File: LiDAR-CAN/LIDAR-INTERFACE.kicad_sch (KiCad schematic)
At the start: 0 parts

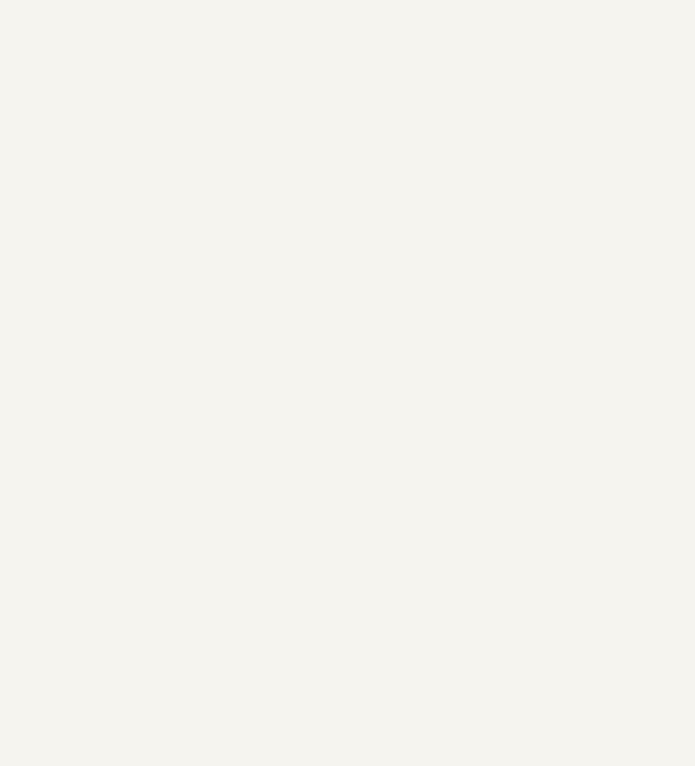
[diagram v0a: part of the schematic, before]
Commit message: Add main components in schematic sheets
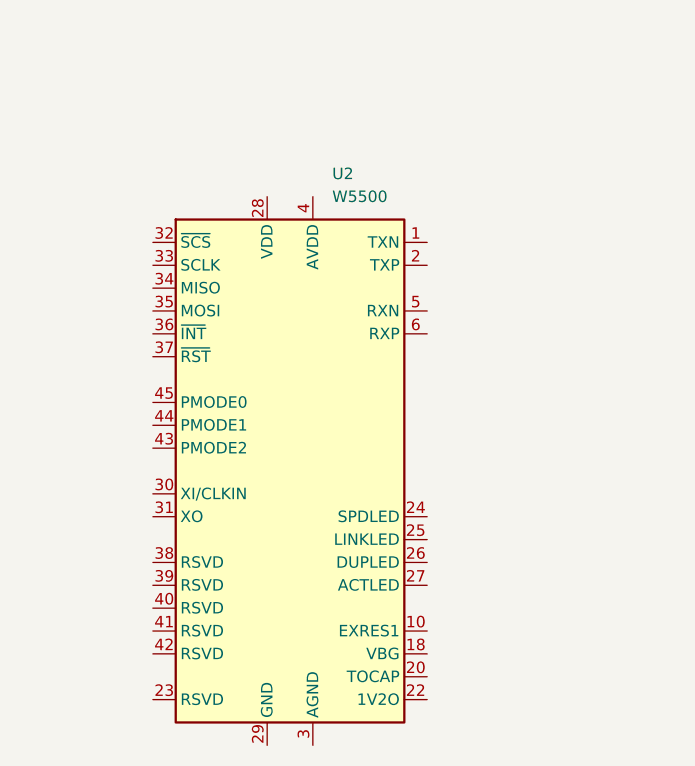
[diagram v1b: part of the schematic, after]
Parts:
- added U2: W5500, Package_QFP:LQFP-48_7x7mm_P0.5mm, symbol Interface_Ethernet:W5500
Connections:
- new net: U2.11 (AVDD), U2.15 (AVDD), U2.17 (AVDD), U2.21 (AVDD), U2.4 (AVDD), U2.8 (AVDD)
- new net: U2.14 (AGND), U2.16 (AGND), U2.19 (AGND), U2.3 (AGND), U2.48 (AGND), U2.9 (AGND)
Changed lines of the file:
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@@
+		)
+	)
+	(symbol
+		(lib_id "Interface_Ethernet:W5500")
+		(at 139.7 91.44 0)
+		(unit 1)
+		(exclude_from_sim no)
+		(in_bom yes)
+		(on_board yes)
+		(dnp no)
+		(fields_autoplaced yes)
+		(property "Reference" "U2"
+			(at 144.3833 58.42 0)
+			(effects
+				(font
+					(size 1.27 1.27)
+				)
+				(justify left)
+			)
+		)
+		(property "Value" "W5500"
+			(at 144.3833 60.96 0)
+			(effects
+				(font
+					(size 1.27 1.27)
+				)
+				(justify left)
+			)
+		)
+		(property "Footprint" "Package_QFP:LQFP-48_7x7mm_P0.5mm"
+			(at 139.7 49.53 0)
+			(effects
+				(font
+					(size 1.27 1.27)
+				)
+				(hide yes)
+			)
+		)
+		(property "Datasheet" "http://wizwiki.net/wiki/lib/exe/fetch.php/products:w5500:w5500_ds_v109e.pdf"
+			(at 139.7 66.04 0)
+			(effects
+				(font
+					(size 1.27 1.27)
+				)
+				(hide yes)
+			)
+		)
+		(property "Description" "10/100Mb SPI Ethernet controller with TCP/IP stack, LQFP-48"
+			(at 139.7 91.44 0)
+			(effects
+				(font
+					(size 1.27 1.27)
+				)
+				(hide yes)
+			)
+		)
+		(pin "32"
+		)
+		(pin "33"
+		)
+		(pin "35"
+		)
+		(pin "36"
+		)
+		(pin "37"
+		)
+		(pin "34"
+		)
+		(pin "15"
+		)
+		(pin "4"
+		)
+		(pin "42"
+		)
+		(pin "23"
+		)
+		(pin "28"
+		)
+		(pin "44"
+		)
+		(pin "29"
+		)
+		(pin "40"
+		)
+		(pin "41"
+		)
+		(pin "17"
+		)
+		(pin "21"
+		)
+		(pin "11"
+		)
+		(pin "8"
+		)
+		(pin "14"
+		)
+		(pin "16"
+		)
+		(pin "45"
+		)
+		(pin "31"
+		)
+		(pin "30"
+		)
+		(pin "38"
+		)
+		(pin "43"
+		)
+		(pin "39"
+		)
+		(pin "5"
+		)
+		(pin "7"
+		)
+		(pin "1"
+		)
+		(pin "22"
+		)
+		(pin "27"
+		)
+		(pin "26"
+		)
+		(pin "12"
+		)
+		(pin "10"
+		)
+		(pin "24"
+		)
+		(pin "3"
+		)
+		(pin "20"
+		)
+		(pin "13"
+		)
+		(pin "47"
+		)
+		(pin "19"
+		)
+		(pin "48"
+		)
+		(pin "9"
+		)
+		(pin "18"
+		)
+		(pin "46"
+		)
+		(pin "2"
+		)
+		(pin "6"
+		)
+		(pin "25"
+		)
+		(instances
+			(project ""
+				(path "/56db6f21-0e4a-4321-bd8a-db37f1842dd9/91fe436f-7e8c-47e0-899c-e39330e04729"
+					(reference "U2")
+					(unit 1)
+				)
+			)
 		)
 	)

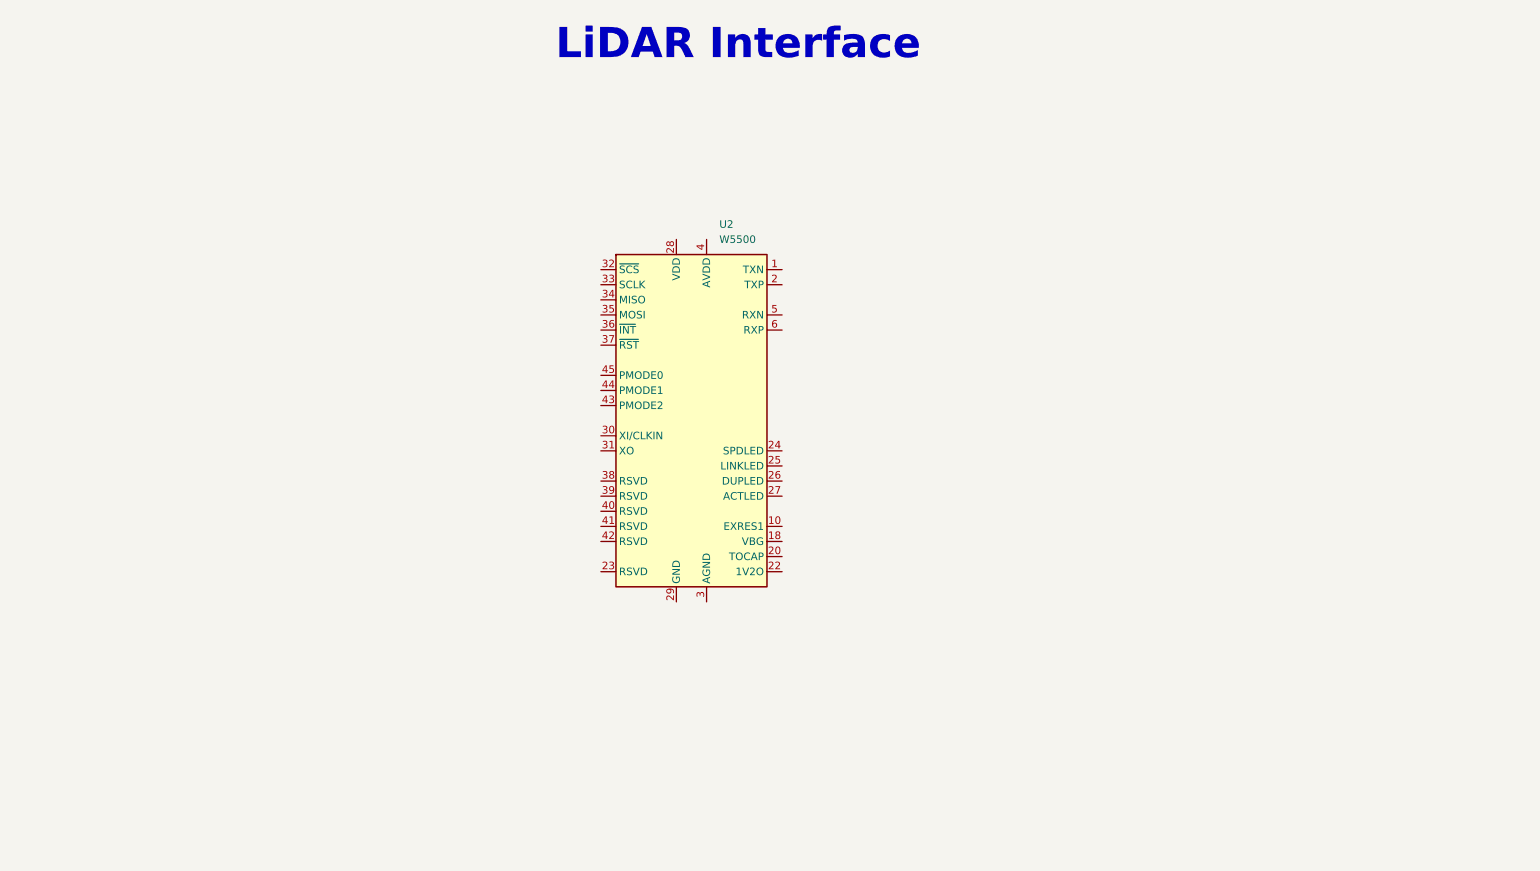
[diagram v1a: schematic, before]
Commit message: Add LiDAR Interface complete circuit
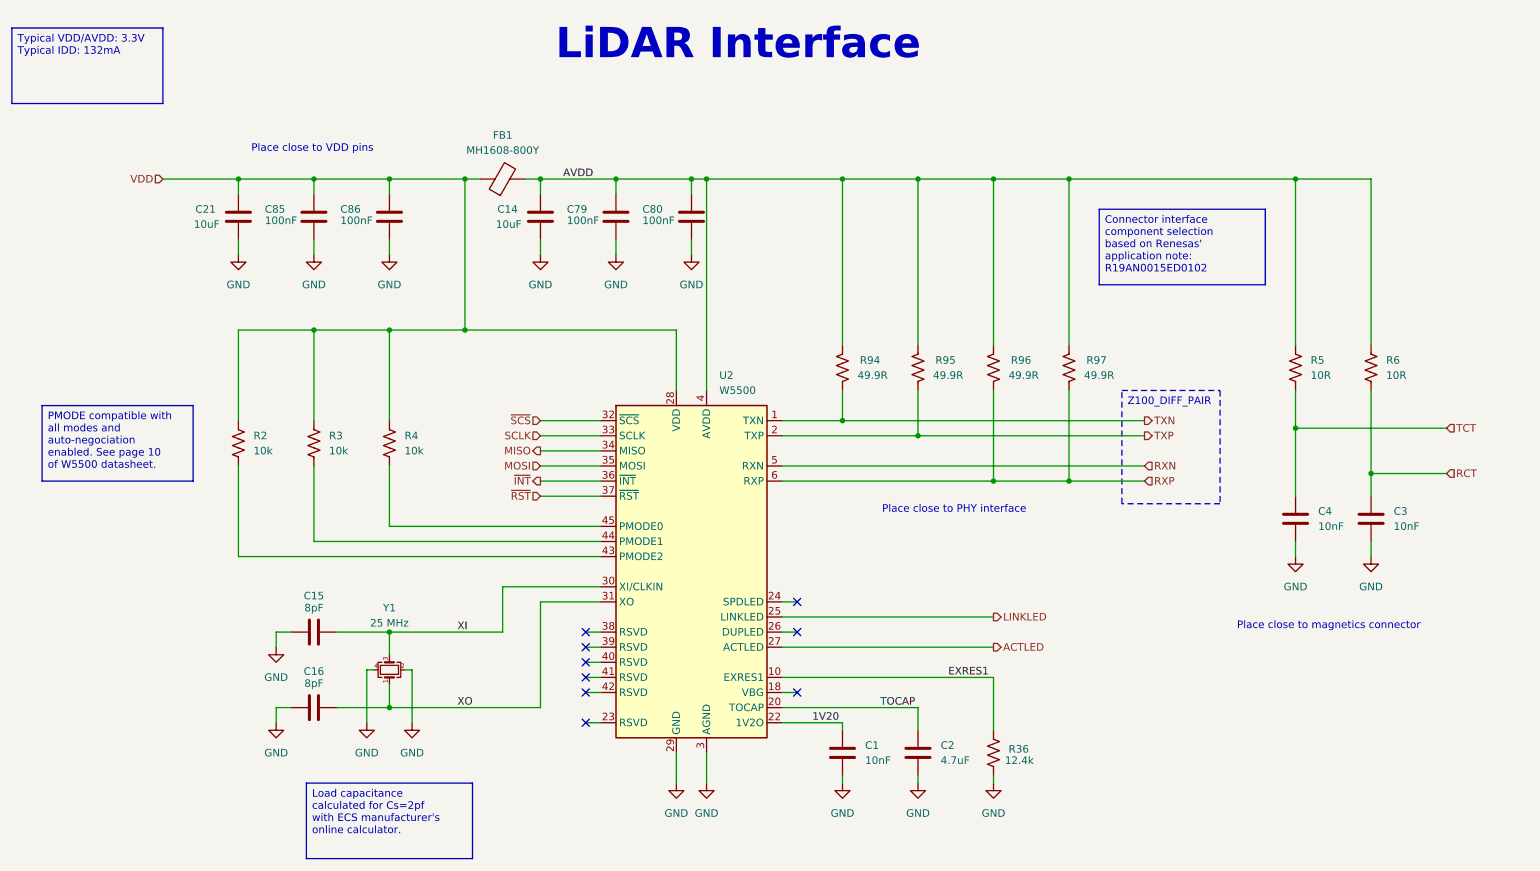
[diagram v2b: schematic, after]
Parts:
- added C1, C3, C4: 10nF, Capacitor_SMD:C_0603_1608Metric, symbol Device:C
- added C14, C21: 10uF, Capacitor_SMD:C_0603_1608Metric, symbol Symbols:CAP CER 10UF 25V X5R 0603
- added C15, C16: 8pF, Capacitor_SMD:C_0603_1608Metric, symbol Symbols:CAP CER 22PF 50V X7R 0603
- added C2: 4.7uF, Capacitor_SMD:C_0603_1608Metric, symbol Device:C
- added C79, C80, C85, C86: 100nF, Capacitor_SMD:C_0603_1608Metric, symbol Symbols:CAP CER 0.1UF 50V X7R 0603
- added FB1: MH1608-800Y, Inductor_SMD:L_0603_1608Metric, symbol Device:FerriteBead
- added R2, R3, R4: 10k, Resistor_SMD:R_0603_1608Metric, symbol Device:R_US
- added R36: 12.4k, Resistor_SMD:R_0603_1608Metric, symbol Symbols:RES 10K OHM 5% 1/10W 0603
- added R5, R6: 10R, Resistor_SMD:R_0603_1608Metric, symbol Device:R_US
- added R94, R95, R96, R97: 49.9R, Resistor_SMD:R_0603_1608Metric, symbol Symbols:RES 1.2K OHM 5% 1/10W 0603
- added Y1: 25 MHz, Crystal:Crystal_SMD_2016-4Pin_2.0x1.6mm, symbol Device:Crystal_GND24_Small
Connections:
- net TXN: now reaches U2.1 (TXN)
- net TXN: now also R94.1
- net EXRES1: now reaches U2.10 (EXRES1)
- net EXRES1: now also R36.2
- net AVDD: now reaches U2.11 (AVDD), U2.15 (AVDD), U2.17 (AVDD), U2.21 (AVDD), U2.4 (AVDD), U2.8 (AVDD)
- net AVDD: now also C14.1, C79.2, C80.2, FB1.2, R5.1, R6.1, R94.2, R95.2, R96.2, R97.2
- net GND: now reaches U2.14 (AGND), U2.16 (AGND), U2.19 (AGND), U2.3 (AGND), U2.48 (AGND), U2.9 (AGND)
- net GND: now also U2.29 (GND), C1.2, C14.2, C15.1, C16.1, C2.2, C21.2, C3.2, C4.2, C79.1, C80.1, C85.1, C86.1, R36.1, Y1.2, Y1.4
- net TXP: now reaches U2.2 (TXP)
- net TXP: now also R95.1
- net TOCAP: now reaches U2.20 (TOCAP)
- net TOCAP: now also C2.1
- net 1V20: now reaches U2.22 (1V2O)
- net 1V20: now also C1.1
- net LINKLED: now reaches U2.25 (LINKLED)
- net ACTLED: now reaches U2.27 (ACTLED)
- net VDD: now reaches U2.28 (VDD)
- net VDD: now also C21.1, C85.2, C86.2, FB1.1, R2.1, R3.1, R4.1
- net XI: now reaches U2.30 (XI/CLKIN)
- net XI: now also C15.2, Y1.3
- net XO: now reaches U2.31 (XO)
- net XO: now also C16.2, Y1.1
- net ~{SCS}: now reaches U2.32 (~{SCS})
- net SCLK: now reaches U2.33 (SCLK)
- net MISO: now reaches U2.34 (MISO)
- net MOSI: now reaches U2.35 (MOSI)
- net ~{INT}: now reaches U2.36 (~{INT})
- net ~{RST}: now reaches U2.37 (~{RST})
- net at U2.43 (PMODE2): now also R2.2
- net at U2.44 (PMODE1): now also R3.2
- net at U2.45 (PMODE0): now also R4.2
- net RXN: now reaches U2.5 (RXN)
- net RXP: now reaches U2.6 (RXP)
- net RXP: now also R96.1, R97.1
- new net RCT: C3.1, R6.2
- new net TCT: C4.1, R5.2
- no-connect marks 0 -> 9
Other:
- note added: "Place close to PHY interface"
- note added: "Place close to VDD pins"
- note added: "Place close to magnetics connector"
- moved on the sheet: U2

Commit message: Add testpoints to LiDAR interface circuit
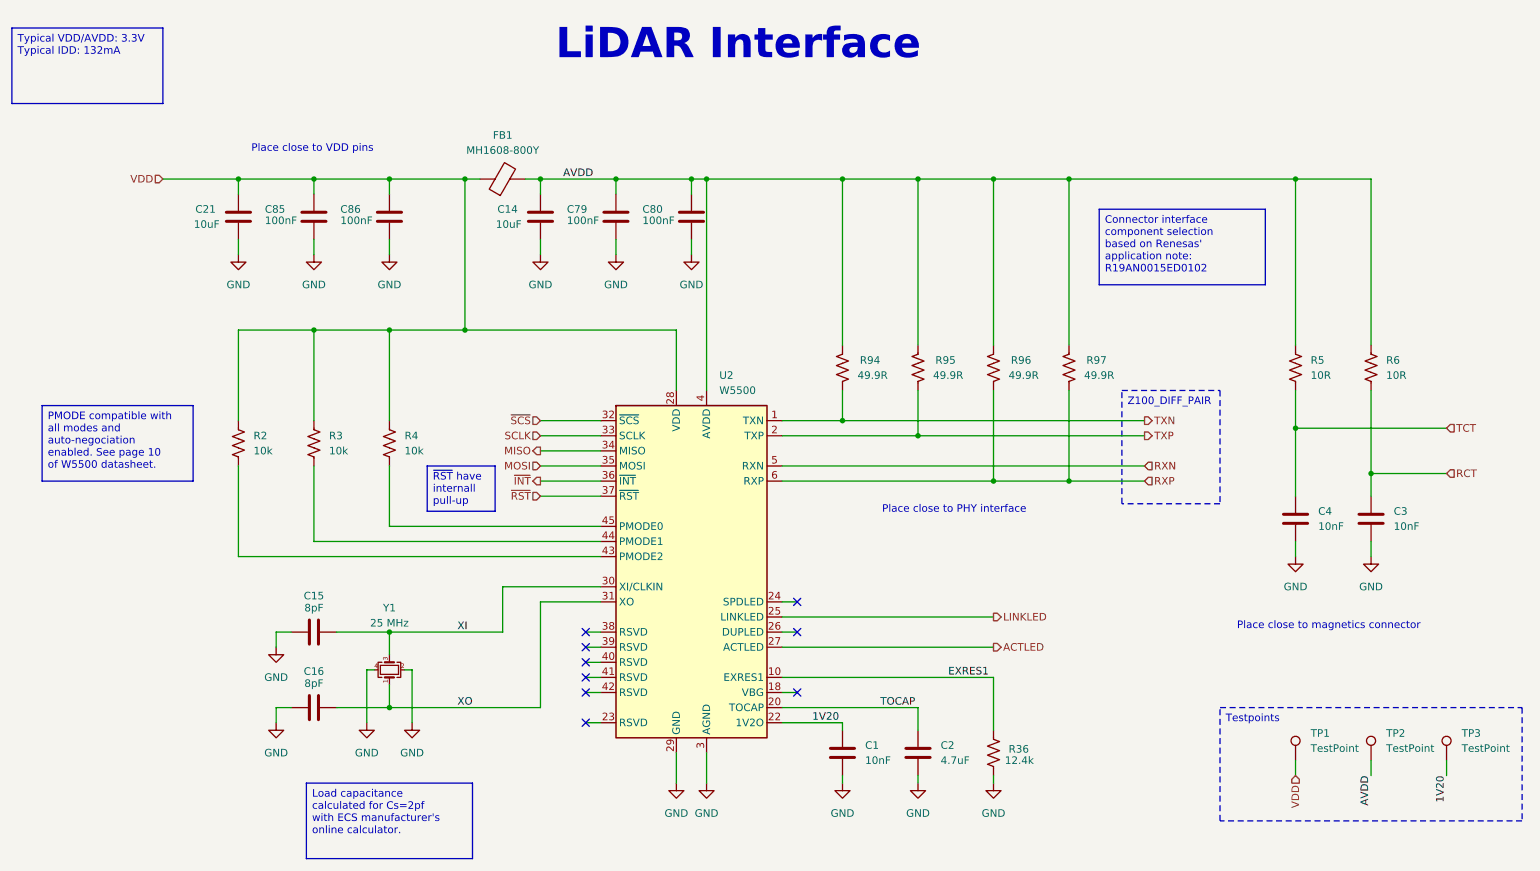
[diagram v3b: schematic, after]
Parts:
- added TP1, TP2, TP3: TestPoint, TestPoint:TestPoint_Pad_D1.5mm, symbol Connector:TestPoint
- U2: MPN (none) -> W5500; Manufacturer (none) -> WIZnet
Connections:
- net 1V20: now also TP3.1
- net AVDD: now also TP2.1
- net VDD: now also TP1.1

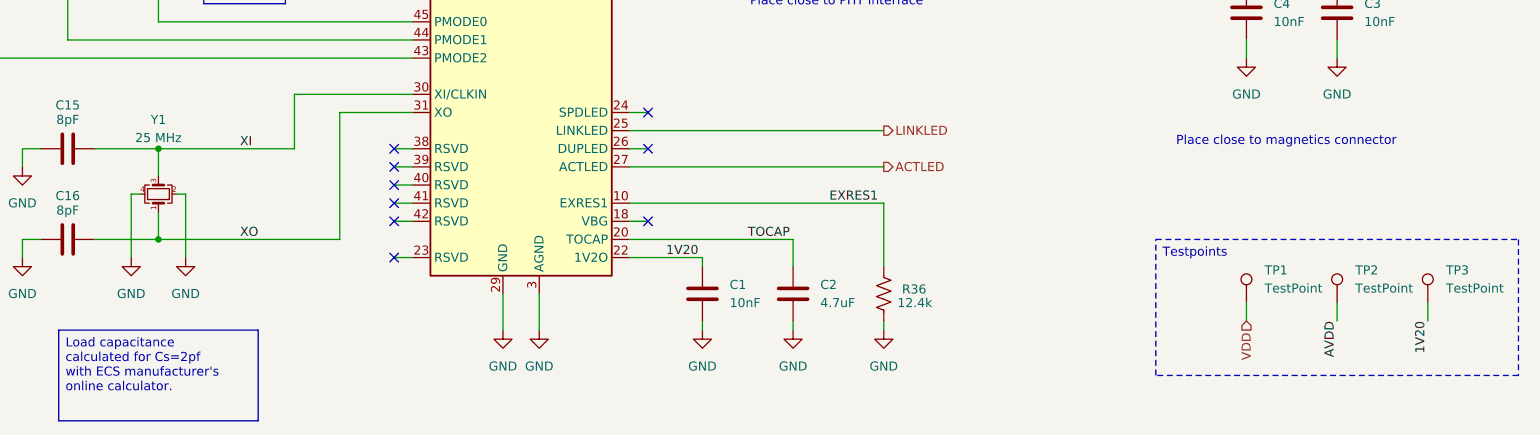
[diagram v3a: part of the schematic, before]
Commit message: Add complete CAN Interface circuit
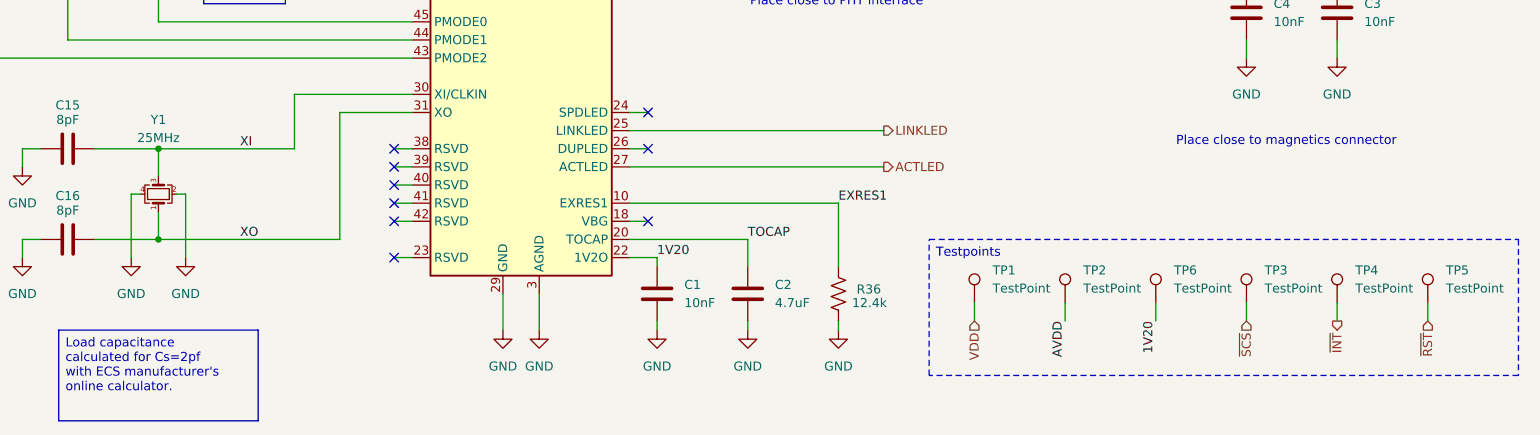
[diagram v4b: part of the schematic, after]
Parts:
- added TP4, TP5, TP6: TestPoint, TestPoint:TestPoint_Pad_D1.5mm, symbol Connector:TestPoint
- Y1: value 25 MHz -> 25MHz
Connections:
- net 1V20: now also TP6.1; no longer TP3.1
- net ~{INT}: now also TP4.1
- net ~{RST}: now also TP5.1
- net ~{SCS}: now also TP3.1
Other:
- moved on the sheet: C1, C2, R36, TP1, TP2, TP3

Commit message: Feature schematic revision 1
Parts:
- renumbered C21 to C14, C85 to C15, C86 to C16, C14 to C17, C79 to C18, C80 to C19, C4 to C20, C3 to C21, C15 to C22, C16 to C23, C1 to C24, C2 to C25, R94 to R17, R95 to R18, R96 to R19, R97 to R20, R5 to R21, R6 to R22, R2 to R23, R3 to R24, R4 to R25, R36 to R26, TP1 to TP17, TP2 to TP18, TP6 to TP19, TP3 to TP20, TP4 to TP21, TP5 to TP22, U2 to U3

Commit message: Start placement of components
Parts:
- TP17, TP18, TP19, TP20, TP21, TP22: footprint TestPoint:TestPoint_Pad_D1.5mm -> TestPoint:TestPoint_Pad_D1.0mm
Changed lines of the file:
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@@
 		(exclude_from_sim no)
 		(in_bom no)
-		(on_board no)
+		(on_board yes)
 		(dnp no)
 		(fields_autoplaced yes)
@@
 			)
 		)
-		(property "Footprint" "TestPoint:TestPoint_Pad_D1.5mm"
+		(property "Footprint" "TestPoint:TestPoint_Pad_D1.0mm"
 			(at 246.38 148.59 0)
 			(effects
@@
 		(exclude_from_sim no)
 		(in_bom no)
-		(on_board no)
+		(on_board yes)
 		(dnp no)
 		(fields_autoplaced yes)
@@
 			)
 		)
-		(property "Footprint" "TestPoint:TestPoint_Pad_D1.5mm"
+		(property "Footprint" "TestPoint:TestPoint_Pad_D1.0mm"
 			(at 233.68 148.59 0)
 			(effects
@@
 		(exclude_from_sim no)
 		(in_bom no)
-		(on_board no)
+		(on_board yes)
 		(dnp no)
 		(fields_autoplaced yes)
@@
 			)
 		)
-		(property "Footprint" "TestPoint:TestPoint_Pad_D1.5mm"
+		(property "Footprint" "TestPoint:TestPoint_Pad_D1.0mm"
 			(at 259.08 148.59 0)
 			(effects
@@
 		(exclude_from_sim no)
 		(in_bom no)
-		(on_board no)
+		(on_board yes)
 		(dnp no)
 		(fields_autoplaced yes)
@@
 			)
 		)
-		(property "Footprint" "TestPoint:TestPoint_Pad_D1.5mm"
+		(property "Footprint" "TestPoint:TestPoint_Pad_D1.0mm"
 			(at 208.28 148.59 0)
 			(effects
@@
 		(exclude_from_sim no)
 		(in_bom no)
-		(on_board no)
+		(on_board yes)
 		(dnp no)
 		(fields_autoplaced yes)
@@
 			)
 		)
-		(property "Footprint" "TestPoint:TestPoint_Pad_D1.5mm"
+		(property "Footprint" "TestPoint:TestPoint_Pad_D1.0mm"
 			(at 271.78 148.59 0)
 			(effects
@@
 		(exclude_from_sim no)
 		(in_bom no)
-		(on_board no)
+		(on_board yes)
 		(dnp no)
 		(fields_autoplaced yes)
@@
 			)
 		)
-		(property "Footprint" "TestPoint:TestPoint_Pad_D1.5mm"
+		(property "Footprint" "TestPoint:TestPoint_Pad_D1.0mm"
 			(at 220.98 148.59 0)
 			(effects
